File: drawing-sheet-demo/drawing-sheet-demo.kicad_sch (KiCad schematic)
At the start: 8 parts, among them J1 Conn_01x02_Pin, U1 LMC555xM

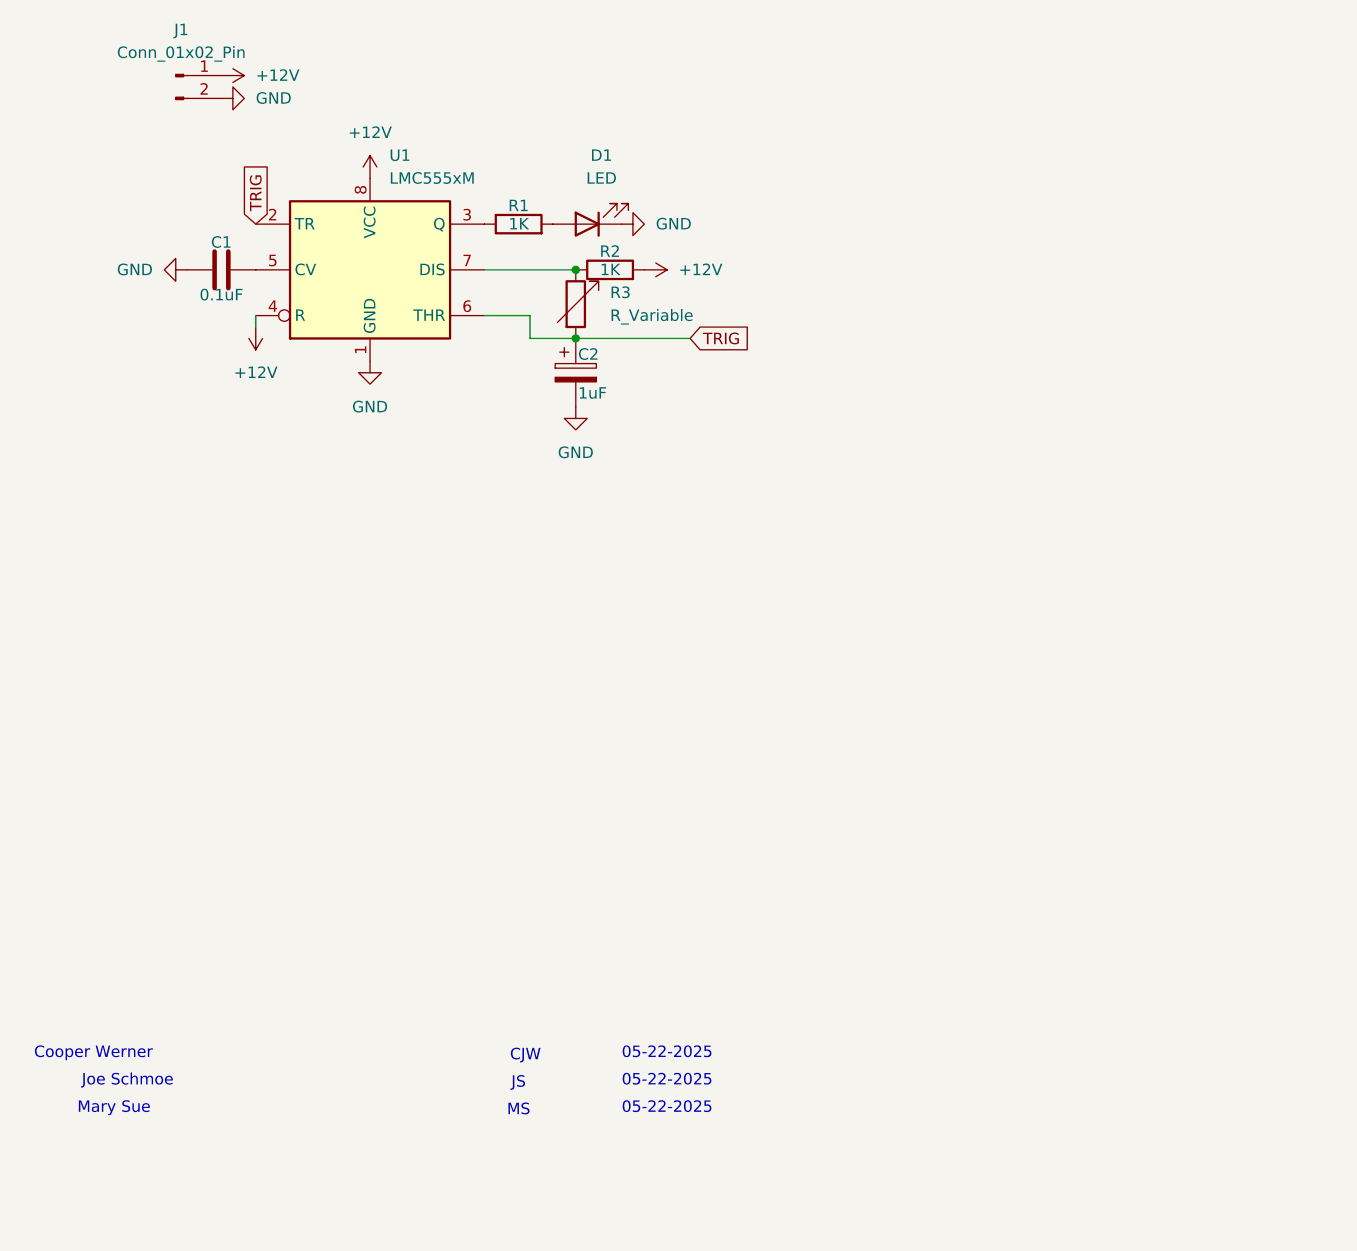
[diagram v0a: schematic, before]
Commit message: better match the Rocket Engine part review process
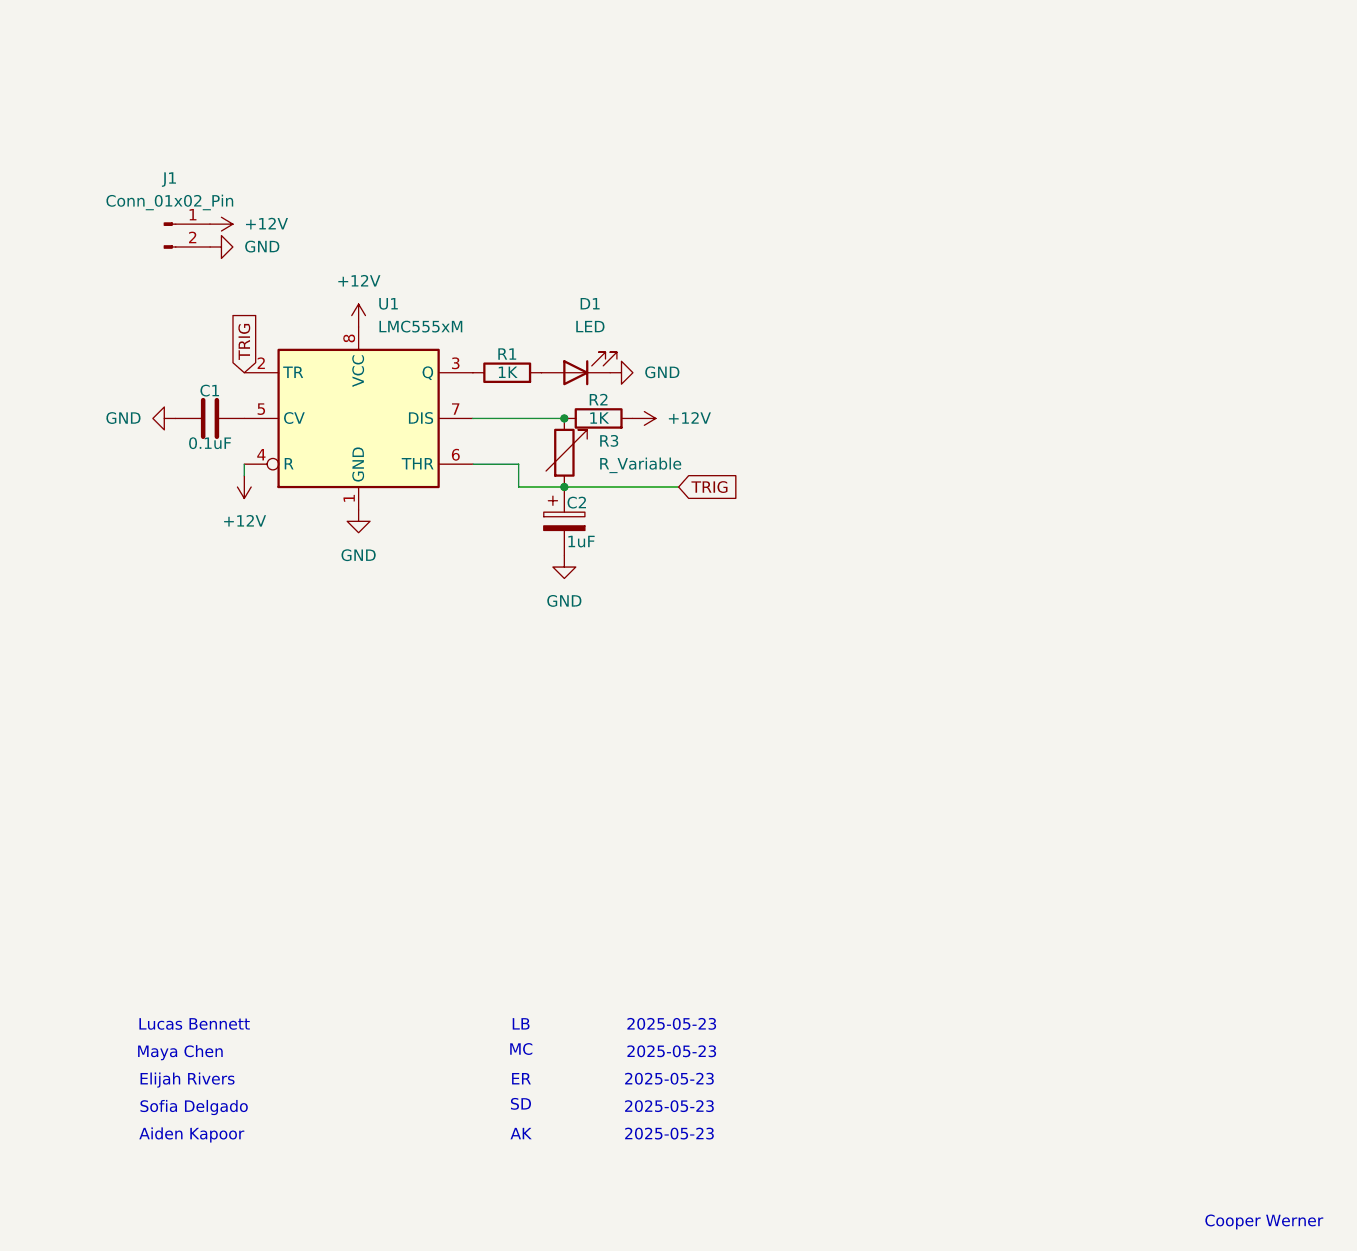
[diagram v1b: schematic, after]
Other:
- note added: "2025-05-23"
- note added: "AK"
- note added: "Aiden Kapoor"
- note added: "ER"
- note added: "Elijah Rivers"
- note added: "LB"
- note added: "Lucas Bennett"
- note added: "MC"
- note added: "Maya Chen"
- note added: "SD"
- note added: "Sofia Delgado"
- note removed: "05-22-2025"
- note removed: "CJW"
- note removed: "JS"
- note removed: "Joe Schmoe"
- note removed: "MS"
- note removed: "Mary Sue"
- moved on the sheet: C1, C2, D1, J1, R1, R2, R3, U1
